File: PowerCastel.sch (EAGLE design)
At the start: 22 parts, among them U1 TPS61090RSAR, U2 MCP73871

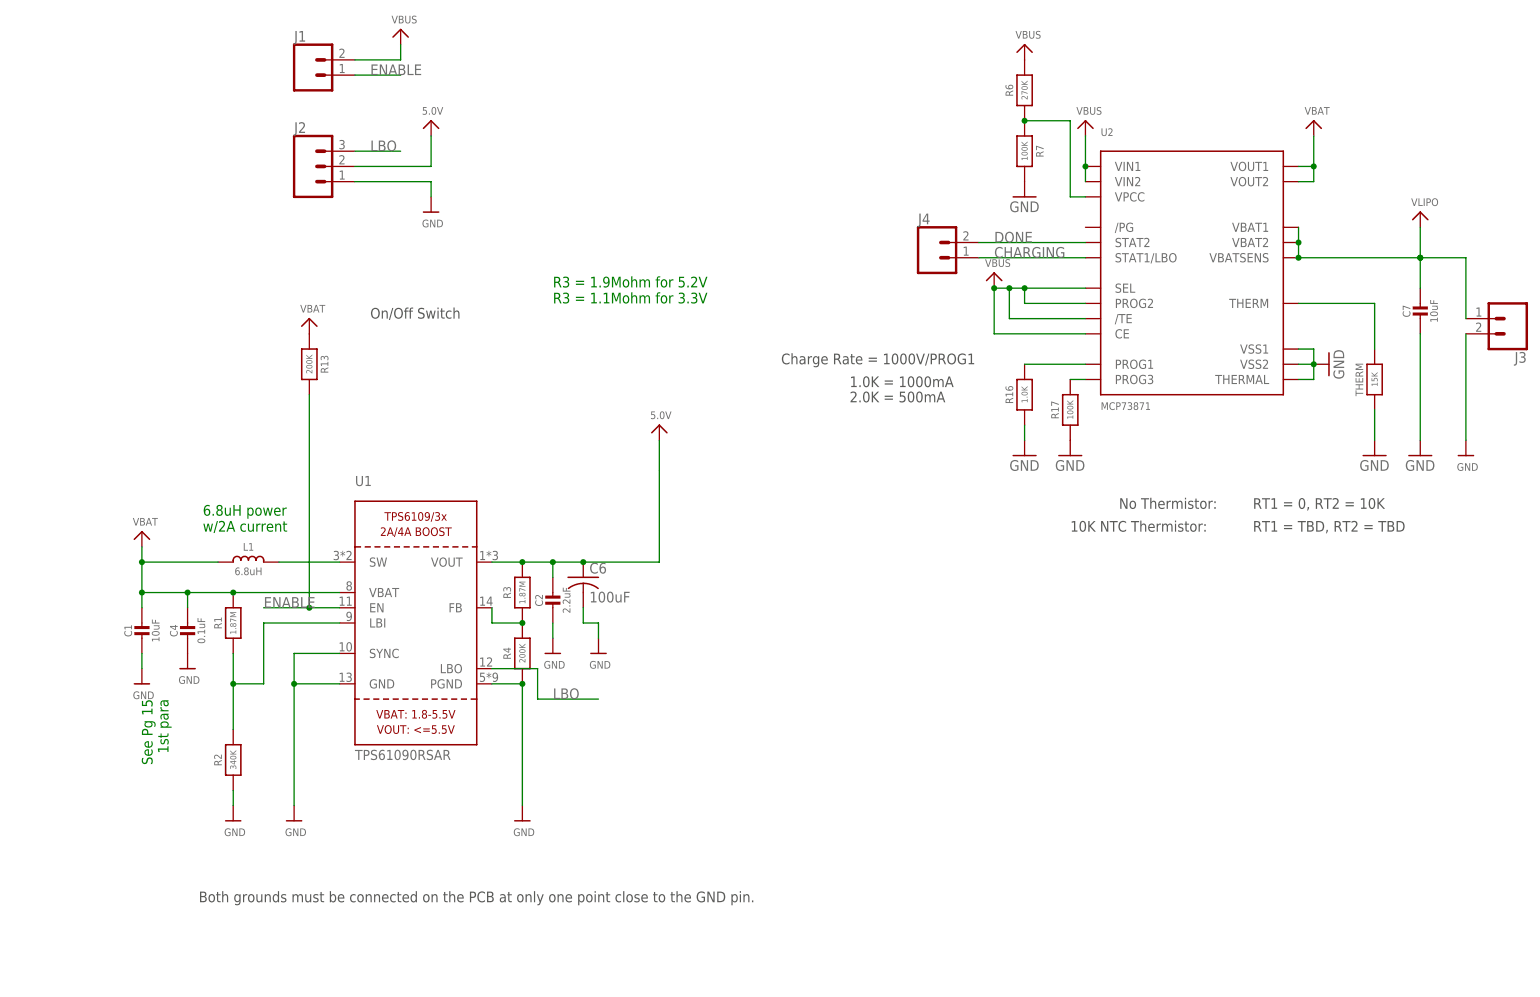
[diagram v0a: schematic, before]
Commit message: Updated design
New design has improved ground plane and has better support for external LEDs.
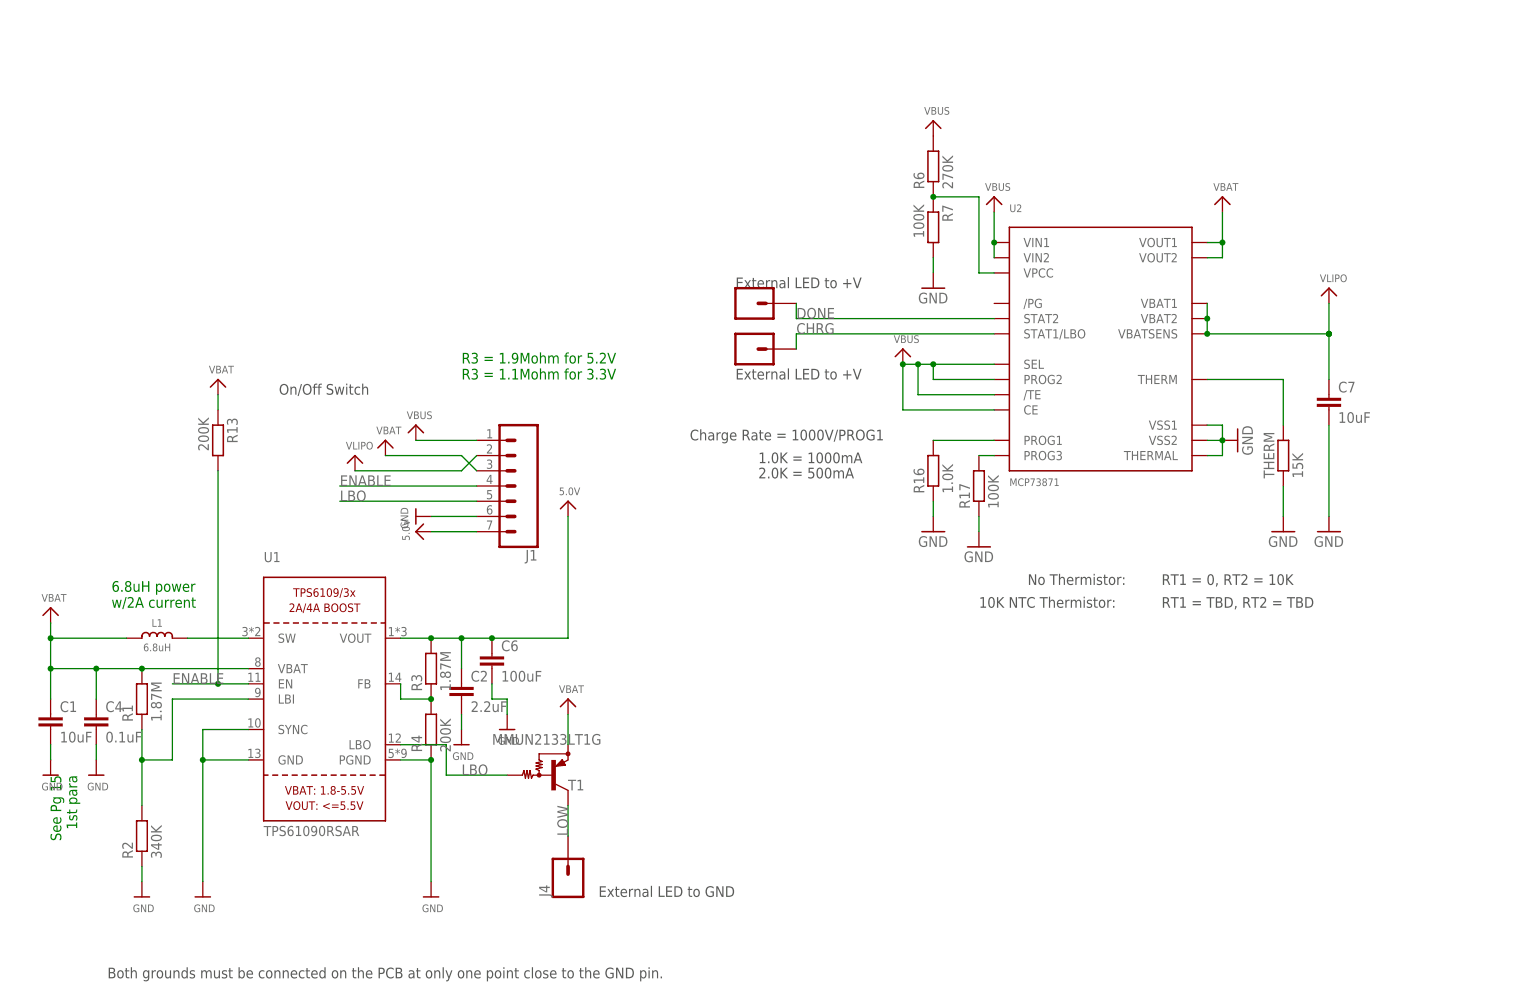
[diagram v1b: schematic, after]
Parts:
- added T1: MMUN2133LT1G, transistor:MUN2114T1-PNP_DRIVER-SC59-BEC
- C1, C2, C7: device microbuilder:CAP_CERAMIC0805-NOOUTLINE -> rcl:C-EUC0603
- C4: device microbuilder:CAP_CERAMIC0805_10MGAP -> rcl:C-EUC0603
- C6: device rcl:C-USC1210 -> rcl:C-EUC0805
- J1: device SparkFun-Connectors:CONN_021X02_NO_SILK -> SparkFun-Connectors:CONN_07NO_SILK
- J2: device SparkFun-Connectors:CONN_031X03_NO_SILK -> SparkFun-Connectors:CONN_01PTH_NO_SILK_YES_STOP
- J3, J4: device SparkFun-Connectors:CONN_021X02_NO_SILK -> SparkFun-Connectors:CONN_01PTH_NO_SILK_YES_STOP
- R1, R2: device microbuilder:RESISTOR_0805MP -> rcl:R-EU_R0603
- R13, R16, R17, R3, R4, R6, R7, THERM: device microbuilder:RESISTOR0805_NOOUTLINE -> rcl:R-EU_R0603
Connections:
- removed net CHARGING: J4.1, U2.STAT1/LBO
- new net CHRG: J3.1, U2.STAT1/LBO
- new net LOW: J4.1, T1.C
- net 5.0V: now also J1.7; no longer J2.2
- net DONE: now also J2.1; no longer J4.2
- net ENABLE: now also J1.4; no longer J1.1
- net GND: now also J1.6; no longer J2.1, J3.2
- net LBO: now also J1.5, T1.B; no longer J2.3
- net VBAT: now also J1.3, T1.E
- net VBUS: now also J1.1; no longer J1.2
- net VLIPO: now also J1.2; no longer J3.1
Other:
- note added: "External LED to +V"
- note added: "External LED to GND"
- moved on the sheet: C1, C2, C4, C6, C7, L1, R1, R13, R16, R17, R2, R3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
